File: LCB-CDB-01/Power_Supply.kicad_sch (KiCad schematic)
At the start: 10 parts, among them J200 USBC_GTC_USB4110-GF-A, U200 TPS73733DCQ

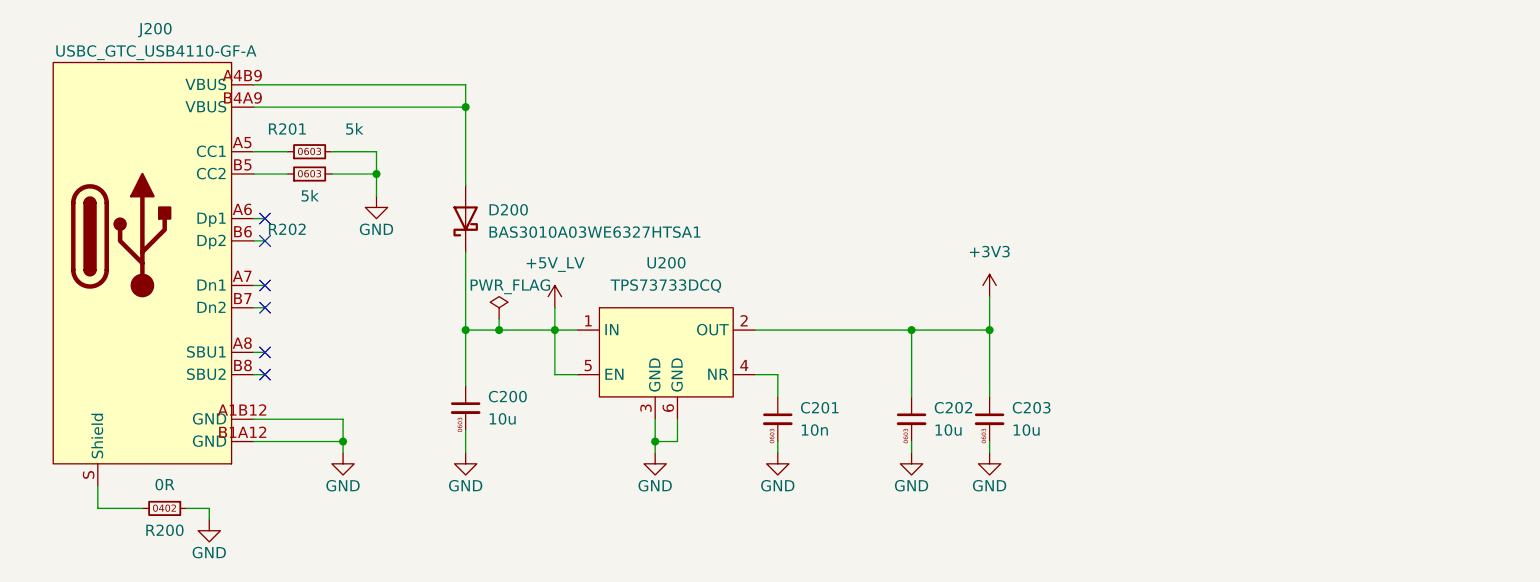
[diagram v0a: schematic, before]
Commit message: update some Rs and Cs names and values, as they can be separate values in KiCad7
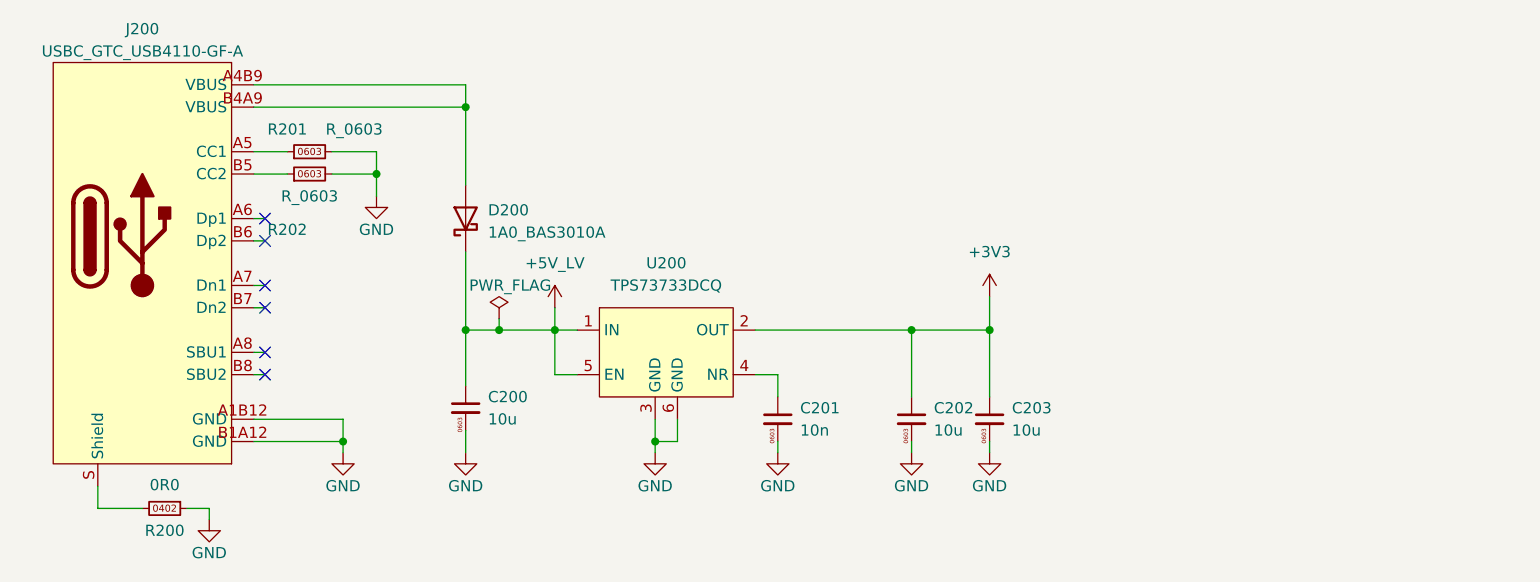
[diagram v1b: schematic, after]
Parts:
- D200: value BAS3010A03WE6327HTSA1 -> 1A0_BAS3010A
- J200: symbol LEA_SymbolLibrary:USBC_GTC_USB4110-GF-A -> LEA_SymbolLibrary:Conn_USBC_GTC_USB4110-GF-A
- R200: value 0R -> 0R0
- R201, R202: value 5k -> R_0603
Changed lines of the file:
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@@
       (effects (font (size 1.27 1.27)))
     )
-    (property "Value" "0R" (at 59.69 82.423 90)
+    (property "Value" "0R0" (at 59.69 82.423 90)
       (effects (font (size 1.27 1.27)))
     )
@@
       (effects (font (size 1.27 1.27)))
     )
-    (property "Value" "5k" (at 76.2 49.53 90)
+    (property "Value" "R_0603" (at 76.2 49.53 90)
       (effects (font (size 1.27 1.27)))
     )
@@
     )
   )
-  (symbol (lib_id "LEA_SymbolLibrary:USBC_GTC_USB4110-GF-A") (at 57.15 57.15 0) (unit 1)
-    (in_bom yes) (on_board yes) (dnp no) (fields_autoplaced)
-    (property "Reference" "J200" (at 58.674 30.48 0)
-      (effects (font (size 1.27 1.27)))
-    )
-    (property "Value" "USBC_GTC_USB4110-GF-A" (at 58.674 33.02 0)
+  (symbol (lib_id "LEA_SymbolLibrary:Conn_USBC_GTC_USB4110-GF-A") (at 57.15 57.15 0) (unit 1)
+    (in_bom yes) (on_board yes) (dnp no) (fields_autoplaced)
+    (property "Reference" "J200" (at 57.15 30.48 0)
+      (effects (font (size 1.27 1.27)))
+    )
+    (property "Value" "USBC_GTC_USB4110-GF-A" (at 57.15 33.02 0)
       (effects (font (size 1.27 1.27)))
     )
@@
       (effects (font (size 1.27 1.27)))
     )
-    (property "Value" "5k" (at 81.28 41.91 90)
+    (property "Value" "R_0603" (at 81.28 41.91 90)
       (effects (font (size 1.27 1.27)))
     )
@@
       (effects (font (size 1.27 1.27)) (justify right))
     )
-    (property "Value" "BAS3010A03WE6327HTSA1" (at 96.52 53.6574 90)
+    (property "Value" "1A0_BAS3010A" (at 96.52 53.6574 90)
       (effects (font (size 1.27 1.27)) (justify right))
     )

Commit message: bump version to 1.1.0
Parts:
- R201, R202: value R_0603 -> 4k7; symbol LEA_SymbolLibrary:R_0603 -> LEA_SymbolLibrary:R_0603__4k7_THICK__1P__75V; Manufacturer (none) -> Vishay; manf# (none) -> CRCW06034K70FKEBC; mouser# (none) -> 71-CRCW06034K70FKEBC
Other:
- title: LCB-CBD-001: Dock -> LCB-CBD-01: Dock
- moved on the sheet: C203
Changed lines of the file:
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@@
   (paper "A4")
   (title_block
-    (title "LCB-CBD-001: Dock")
-    (date "2022-08-12")
-    (rev "0.1")
+    (title "LCB-CBD-01: Dock")
+    (date "2023-04-13")
+    (rev "1.1.0")
     (company "PADERBORN UNIVERSITY DEPARTMENT OF POWER ELECTRONICS AND ELECTRICAL DRIVES")
   )
   (junction (at 115.57 77.47) (diameter 0) (color 0 0 0 0)
   )
-  (junction (at 153.67 64.77) (diameter 0) (color 0 0 0 0)
+  (junction (at 154.94 64.77) (diameter 0) (color 0 0 0 0)
   )
   (junction (at 93.98 39.37) (diameter 0) (color 0 0 0 0)
@@
     (stroke (width 0) (type default))
   )
-  (wire (pts (xy 153.67 64.77) (xy 153.67 72.39))
-    (stroke (width 0) (type default))
-  )
-  (wire (pts (xy 153.67 64.77) (xy 153.67 60.96))
+  (wire (pts (xy 154.94 64.77) (xy 154.94 72.39))
+    (stroke (width 0) (type default))
+  )
+  (wire (pts (xy 154.94 64.77) (xy 154.94 60.96))
     (stroke (width 0) (type default))
   )
@@
     (stroke (width 0) (type default))
   )
-  (wire (pts (xy 153.67 77.47) (xy 153.67 78.74))
+  (wire (pts (xy 154.94 77.47) (xy 154.94 78.74))
     (stroke (width 0) (type default))
   )
@@
     (stroke (width 0) (type default))
   )
-  (wire (pts (xy 144.78 64.77) (xy 153.67 64.77))
+  (wire (pts (xy 144.78 64.77) (xy 154.94 64.77))
     (stroke (width 0) (type default))
   )
@@
     )
   )
-  (symbol (lib_id "LEA_SymbolLibrary:C_0603__10u_X5R_10P__25V") (at 153.67 74.93 0) (unit 1)
+  (symbol (lib_id "LEA_SymbolLibrary:C_0603__10u_X5R_10P__25V") (at 154.94 74.93 0) (unit 1)
     (in_bom yes) (on_board yes) (dnp no) (fields_autoplaced)
-    (property "Reference" "C203" (at 156.21 73.6662 0)
+    (property "Reference" "C203" (at 157.48 73.6662 0)
       (effects (font (size 1.27 1.27)) (justify left))
     )
-    (property "Value" "10u" (at 156.21 76.2062 0)
+    (property "Value" "10u" (at 157.48 76.2062 0)
       (effects (font (size 1.27 1.27)) (justify left))
     )
-    (property "Footprint" "LEA_FootprintLibrary:C_0603" (at 153.67 64.77 0)
-      (effects (font (size 1.27 1.27)) hide)
-    )
-    (property "Datasheet" "" (at 153.67 74.93 0)
-      (effects (font (size 1.27 1.27)) hide)
-    )
-    (property "Mfr. No" "" (at 153.67 74.93 0)
-      (effects (font (size 1.27 1.27)) hide)
-    )
-    (property "Manufacturer" "Murata" (at 153.67 74.93 0)
-      (effects (font (size 1.27 1.27)) hide)
-    )
-    (property "Mouser No" "" (at 153.67 74.93 0)
-      (effects (font (size 1.27 1.27)) hide)
-    )
-    (property "manf#" "GRM188R61E106KA3D" (at 153.67 74.93 0)
-      (effects (font (size 1.27 1.27)) hide)
-    )
-    (property "mouser#" "81-GRM188R61E106KA3D" (at 153.67 74.93 0)
+    (property "Footprint" "LEA_FootprintLibrary:C_0603" (at 154.94 64.77 0)
+      (effects (font (size 1.27 1.27)) hide)
+    )
+    (property "Datasheet" "" (at 154.94 74.93 0)
+      (effects (font (size 1.27 1.27)) hide)
+    )
+    (property "Mfr. No" "" (at 154.94 74.93 0)
+      (effects (font (size 1.27 1.27)) hide)
+    )
+    (property "Manufacturer" "Murata" (at 154.94 74.93 0)
+      (effects (font (size 1.27 1.27)) hide)
+    )
+    (property "Mouser No" "" (at 154.94 74.93 0)
+      (effects (font (size 1.27 1.27)) hide)
+    )
+    (property "manf#" "GRM188R61E106KA3D" (at 154.94 74.93 0)
+      (effects (font (size 1.27 1.27)) hide)
+    )
+    (property "mouser#" "81-GRM188R61E106KA3D" (at 154.94 74.93 0)
       (effects (font (size 1.27 1.27)) hide)
     )
@@
     )
   )
-  (symbol (lib_id "LEA_SymbolLibrary:GND") (at 153.67 78.74 0) (unit 1)
-    (in_bom yes) (on_board yes) (dnp no)
-    (property "Reference" "#PWR067" (at 156.21 81.28 90)
-      (effects (font (size 1.27 1.27)) hide)
-    )
-    (property "Value" "GND" (at 153.67 82.55 0)
-      (effects (font (size 1.27 1.27)))
-    )
-    (property "Footprint" "" (at 153.67 78.74 0)
-      (effects (font (size 1.27 1.27)) hide)
-    )
-    (property "Datasheet" "" (at 153.67 78.74 0)
+  (symbol (lib_id "LEA_SymbolLibrary:GND") (at 154.94 78.74 0) (unit 1)
+    (in_bom yes) (on_board yes) (dnp no)
+    (property "Reference" "#PWR067" (at 157.48 81.28 90)
+      (effects (font (size 1.27 1.27)) hide)
+    )
+    (property "Value" "GND" (at 154.94 82.55 0)
+      (effects (font (size 1.27 1.27)))
+    )
+    (property "Footprint" "" (at 154.94 78.74 0)
+      (effects (font (size 1.27 1.27)) hide)
+    )
+    (property "Datasheet" "" (at 154.94 78.74 0)
       (effects (font (size 1.27 1.27)) hide)
     )
@@
     )
   )
-  (symbol (lib_id "LEA_SymbolLibrary:R_0603") (at 76.2 46.99 90) (unit 1)
-    (in_bom yes) (on_board yes) (dnp no)
-    (property "Reference" "R202" (at 73.66 53.34 90)
-      (effects (font (size 1.27 1.27)))
-    )
-    (property "Value" "R_0603" (at 76.2 49.53 90)
+  (symbol (lib_id "LEA_SymbolLibrary:R_0603__4k7_THICK__1P__75V") (at 76.2 46.99 90) (unit 1)
+    (in_bom yes) (on_board yes) (dnp no)
+    (property "Reference" "R202" (at 73.66 49.53 90)
+      (effects (font (size 1.27 1.27)))
+    )
+    (property "Value" "4k7" (at 78.74 49.53 90)
       (effects (font (size 1.27 1.27)))
     )
@@
       (effects (font (size 1.27 1.27)) hide)
     )
-    (property "Manufacturer" "" (at 76.2 46.99 0)
+    (property "Manufacturer" "Vishay" (at 76.2 46.99 0)
       (effects (font (size 1.27 1.27)) hide)
     )
     (property "Mouser No" "" (at 76.2 46.99 0)
+      (effects (font (size 1.27 1.27)) hide)
+    )
+    (property "manf#" "CRCW06034K70FKEBC" (at 76.2 46.99 0)
+      (effects (font (size 1.27 1.27)) hide)
+    )
+    (property "mouser#" "71-CRCW06034K70FKEBC" (at 76.2 46.99 0)
       (effects (font (size 1.27 1.27)) hide)
     )
@@
     )
   )
-  (symbol (lib_id "LEA_SymbolLibrary:R_0603") (at 76.2 44.45 90) (unit 1)
+  (symbol (lib_id "LEA_SymbolLibrary:R_0603__4k7_THICK__1P__75V") (at 76.2 44.45 90) (unit 1)
     (in_bom yes) (on_board yes) (dnp no)
     (property "Reference" "R201" (at 73.66 41.91 90)
       (effects (font (size 1.27 1.27)))
     )
-    (property "Value" "R_0603" (at 81.28 41.91 90)
+    (property "Value" "4k7" (at 78.74 41.91 90)
       (effects (font (size 1.27 1.27)))
     )
@@
       (effects (font (size 1.27 1.27)) hide)
     )
-    (property "Manufacturer" "" (at 76.2 44.45 0)
+    (property "Manufacturer" "Vishay" (at 76.2 44.45 0)
       (effects (font (size 1.27 1.27)) hide)
     )
     (property "Mouser No" "" (at 76.2 44.45 0)
+      (effects (font (size 1.27 1.27)) hide)
+    )
+    (property "manf#" "CRCW06034K70FKEBC" (at 76.2 44.45 0)
+      (effects (font (size 1.27 1.27)) hide)
+    )
+    (property "mouser#" "71-CRCW06034K70FKEBC" (at 76.2 44.45 0)
       (effects (font (size 1.27 1.27)) hide)
     )
@@
     )
   )
-  (symbol (lib_id "LEA_SymbolLibrary:+3V3") (at 153.67 60.96 0) (unit 1)
+  (symbol (lib_id "LEA_SymbolLibrary:+3V3") (at 154.94 60.96 0) (unit 1)
     (in_bom yes) (on_board yes) (dnp no) (fields_autoplaced)
-    (property "Reference" "#PWR066" (at 154.94 60.96 90)
-      (effects (font (size 1.27 1.27)) hide)
-    )
-    (property "Value" "+3V3" (at 153.67 55.88 0)
-      (effects (font (size 1.27 1.27)))
-    )
-    (property "Footprint" "" (at 153.67 60.96 0)
-      (effects (font (size 1.27 1.27)) hide)
-    )
-    (property "Datasheet" "" (at 153.67 60.96 0)
-      (effects (font (size 1.27 1.27)) hide)
-    )
+    (property "Reference" "#PWR066" (at 156.21 60.96 90)
+      (effects (font (size 1.27 1.27)) hide)
+    )
+    (property "Value" "+3V3" (at 154.94 55.88 0)
+      (effects (font (size 1.27 1.27)))
+    )
+    (property "Footprint" "" (at 154.94 60.96 0)
+      (effects (font (size 1.27 1.27)) hide)
+    )
+    (property "Datasheet" "" (at 154.94 60.96 0)
+      (effects (font (size 1.27 1.27)) hide)
+    )

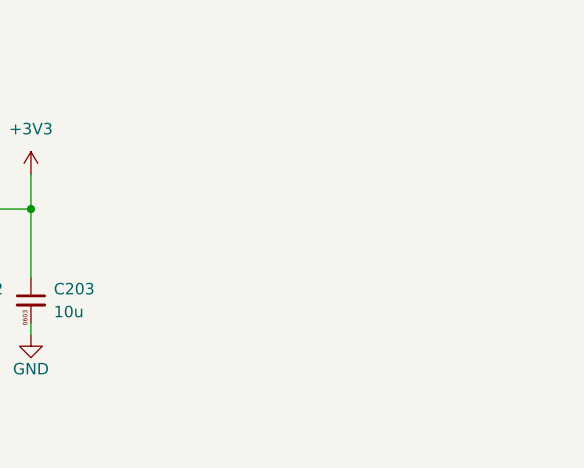
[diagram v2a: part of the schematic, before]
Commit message: update: Issue fix - 3V supply for potentiometers
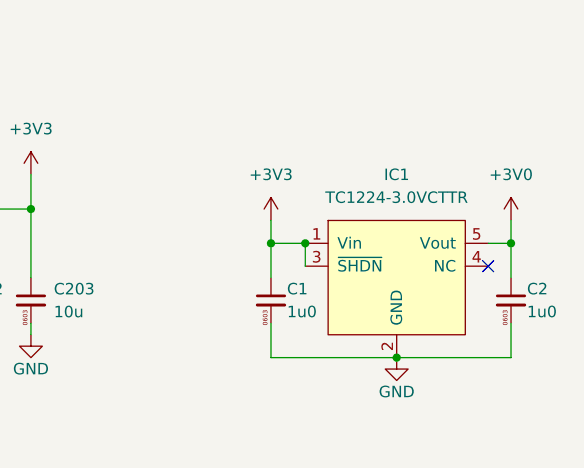
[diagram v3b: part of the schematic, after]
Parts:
- added C1, C2: 1u0, LEA_FootprintLibrary:C_0603, symbol LEA_SymbolLibrary:C_0603__1u0_X5R_10P__50V
- added IC1: TC1224-3.0VCTTR, LEA_FootprintLibrary:SOT-23-5_Microchip, symbol LEA_SymbolLibrary:LDO_TC1224-3.0VCTTR
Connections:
- net +3V3: now also C1.1, IC1.1 (Vin), IC1.3 (~{SHDN})
- net GND: now also C1.2, C2.2, IC1.2 (GND)
- new net +3V0: C2.1, IC1.5 (Vout)
- no-connect marks 6 -> 7

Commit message: update symbols without simulation models
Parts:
- D200: Mfr. No BAS3010A03WE6327HTSA1 -> (none); Mouser No 726-BAS3010A-03WE6 -> (none)
- J200: Mfr. No USB4110-GF-A -> (none); Mouser No 640-USB4110-GF-A -> (none)
- U200: Mouser No. 595-TPS73733DCQG4 -> (none)
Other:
- title: LCB-CBD-01: Dock -> LCB-CDB-01: Dock Board
